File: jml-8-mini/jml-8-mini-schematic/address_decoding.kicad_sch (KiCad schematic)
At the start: 9 parts, among them J5 Address Decoding, U6 74LS04, U7 CD74HCT4514E, U8 74LS139, U9 74LS32

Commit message: change some footprints
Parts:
- U6, U9: footprint Package_DIP:DIP-14_W7.62mm_LongPads -> Package_DIP:DIP-14_W7.62mm_Socket_LongPads
- U7: footprint Package_DIP:DIP-24_W15.24mm_LongPads -> Package_DIP:DIP-24_W15.24mm_Socket_LongPads
- U8: footprint Package_DIP:DIP-16_W7.62mm_LongPads -> Package_DIP:DIP-16_W7.62mm_Socket_LongPads
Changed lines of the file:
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@@
       (effects (font (size 1.27 1.27)))
     )
-    (property "Footprint" "Package_DIP:DIP-14_W7.62mm_LongPads" (at 78.74 46.99 0)
+    (property "Footprint" "Package_DIP:DIP-14_W7.62mm_Socket_LongPads" (at 78.74 46.99 0)
       (effects (font (size 1.27 1.27)) hide)
     )
@@
       (effects (font (size 1.27 1.27)))
     )
-    (property "Footprint" "Package_DIP:DIP-14_W7.62mm_LongPads" (at 116.84 73.66 0)
+    (property "Footprint" "Package_DIP:DIP-14_W7.62mm_Socket_LongPads" (at 116.84 73.66 0)
       (effects (font (size 1.27 1.27)) hide)
     )
@@
       (effects (font (size 1.27 1.27)))
     )
-    (property "Footprint" "Package_DIP:DIP-14_W7.62mm_LongPads" (at 127 104.14 0)
+    (property "Footprint" "Package_DIP:DIP-14_W7.62mm_Socket_LongPads" (at 127 104.14 0)
       (effects (font (size 1.27 1.27)) hide)
     )
@@
       (effects (font (size 1.27 1.27)) (justify left))
     )
-    (property "Footprint" "Package_DIP:DIP-16_W7.62mm_LongPads" (at 256.54 129.54 0)
+    (property "Footprint" "Package_DIP:DIP-16_W7.62mm_Socket_LongPads" (at 256.54 129.54 0)
       (effects (font (size 1.27 1.27)) hide)
     )
@@
       (effects (font (size 1.27 1.27)) (justify left))
     )
-    (property "Footprint" "Package_DIP:DIP-24_W15.24mm_LongPads" (at 21.59 85.09 0)
+    (property "Footprint" "Package_DIP:DIP-24_W15.24mm_Socket_LongPads" (at 21.59 85.09 0)
       (effects (font (size 1.27 1.27)) hide)
     )
@@
       (effects (font (size 1.27 1.27)))
     )
-    (property "Footprint" "Package_DIP:DIP-14_W7.62mm_LongPads" (at 251.46 83.185 0)
+    (property "Footprint" "Package_DIP:DIP-14_W7.62mm_Socket_LongPads" (at 251.46 83.185 0)
       (effects (font (size 1.27 1.27)) hide)
     )
@@
       (effects (font (size 1.27 1.27)))
     )
-    (property "Footprint" "Package_DIP:DIP-14_W7.62mm_LongPads" (at 271.78 83.185 0)
+    (property "Footprint" "Package_DIP:DIP-14_W7.62mm_Socket_LongPads" (at 271.78 83.185 0)
       (effects (font (size 1.27 1.27)) hide)
     )
@@
       (effects (font (size 1.27 1.27)))
     )
-    (property "Footprint" "Package_DIP:DIP-14_W7.62mm_LongPads" (at 143.51 29.21 0)
+    (property "Footprint" "Package_DIP:DIP-14_W7.62mm_Socket_LongPads" (at 143.51 29.21 0)
       (effects (font (size 1.27 1.27)) hide)
     )
@@
       (effects (font (size 1.27 1.27)))
     )
-    (property "Footprint" "Package_DIP:DIP-14_W7.62mm_LongPads" (at 261.62 83.185 0)
+    (property "Footprint" "Package_DIP:DIP-14_W7.62mm_Socket_LongPads" (at 261.62 83.185 0)
       (effects (font (size 1.27 1.27)) hide)
     )
@@
       (effects (font (size 1.27 1.27)) (justify left))
     )
-    (property "Footprint" "Package_DIP:DIP-16_W7.62mm_LongPads" (at 83.82 160.02 0)
+    (property "Footprint" "Package_DIP:DIP-16_W7.62mm_Socket_LongPads" (at 83.82 160.02 0)
       (effects (font (size 1.27 1.27)) hide)
     )
@@
       (effects (font (size 1.27 1.27)))
     )
-    (property "Footprint" "Package_DIP:DIP-14_W7.62mm_LongPads" (at 143.51 44.45 0)
+    (property "Footprint" "Package_DIP:DIP-14_W7.62mm_Socket_LongPads" (at 143.51 44.45 0)
       (effects (font (size 1.27 1.27)) hide)
     )
@@
       (effects (font (size 1.27 1.27)))
     )
-    (property "Footprint" "Package_DIP:DIP-14_W7.62mm_LongPads" (at 241.3 83.185 0)
+    (property "Footprint" "Package_DIP:DIP-14_W7.62mm_Socket_LongPads" (at 241.3 83.185 0)
       (effects (font (size 1.27 1.27)) hide)
     )
@@
       (effects (font (size 1.27 1.27)) (justify left))
     )
-    (property "Footprint" "Package_DIP:DIP-14_W7.62mm_LongPads" (at 262.89 44.45 0)
+    (property "Footprint" "Package_DIP:DIP-14_W7.62mm_Socket_LongPads" (at 262.89 44.45 0)
       (effects (font (size 1.27 1.27)) hide)
     )
@@
       (effects (font (size 1.27 1.27)) (justify left))
     )
-    (property "Footprint" "Package_DIP:DIP-14_W7.62mm_LongPads" (at 237.49 44.45 0)
-      (effects (font (size 1.27 1.27)) hide)
-    )
+    (property "Footprint" "Package_DIP:DIP-14_W7.62mm_Socket_LongPads" (at 237.49 44.45 0)
+      (effects (font (size 1.27 1.27)) hide)
+    )

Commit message: lots of updates to schematic to make pcb routing easier, start on pcb design
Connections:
- net A15: now also U9.1; no longer U9.9
- net A5: now also U7.3 (A1); no longer U7.2 (A0)
- net A6: no longer U7.3 (A1)
- net Q0: now also J5.20 (Pin_20); no longer J5.17 (Pin_17)
- net Q1: now also J5.19 (Pin_19), U9.10; no longer J5.18 (Pin_18), U9.5
- net Q2: now also J5.18 (Pin_18), U9.13; no longer J5.19 (Pin_19), U9.2
- net Q3: now also J5.17 (Pin_17); no longer J5.20 (Pin_20)
- net Y0: now also J5.2 (Pin_2), U9.12, U9.9; no longer J5.1 (Pin_1), U9.1, U9.4
- net Y1: now also J5.4 (Pin_4); no longer J5.2 (Pin_2)
- net Y10: now also J5.10 (Pin_10); no longer J5.11 (Pin_11)
- net Y11: now also J5.9 (Pin_9); no longer J5.12 (Pin_12)
- net Y12: now also J5.3 (Pin_3); no longer J5.13 (Pin_13)
- net Y13: now also J5.1 (Pin_1); no longer J5.14 (Pin_14)
- net Y14: now also J5.6 (Pin_6); no longer J5.15 (Pin_15)
- net Y15: now also J5.5 (Pin_5); no longer J5.16 (Pin_16)
- net Y2: now also J5.11 (Pin_11); no longer J5.3 (Pin_3)
- net Y3: now also J5.12 (Pin_12); no longer J5.4 (Pin_4)
- net Y4: now also J5.13 (Pin_13); no longer J5.5 (Pin_5)
- net Y5: now also J5.14 (Pin_14); no longer J5.6 (Pin_6)
- net Y6: now also J5.15 (Pin_15); no longer J5.7 (Pin_7)
- net Y7: now also J5.16 (Pin_16); no longer J5.8 (Pin_8)
- net Y8: now also J5.8 (Pin_8); no longer J5.9 (Pin_9)
- net Y9: now also J5.7 (Pin_7); no longer J5.10 (Pin_10)
- net ~{CTC}: now also U9.11; no longer U9.3
- net ~{MREQ}: now also U9.2, U9.4; no longer U9.10, U9.12
- net ~{RAM}: now also U9.6; no longer U9.11
- net ~{ROM}: now also U9.3; no longer U9.8
- net ~{SIO}: now also U9.8; no longer U9.6
- net ~{A15}: now reaches U6.2
- net ~{A15}: now also U9.5; no longer U9.13
- new net A4: U7.2 (A0)
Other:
- note added: "Address Decoding Breakout"
- note added: "Power"
- moved on the sheet: U6G, U9E

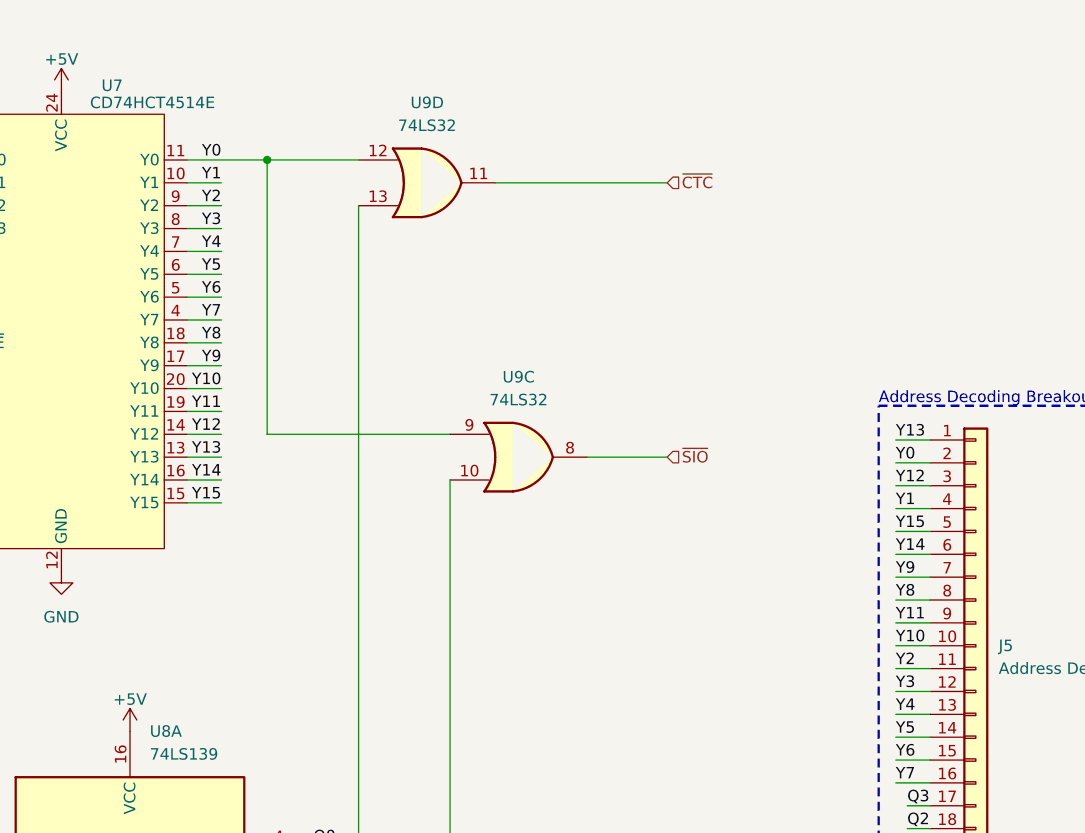
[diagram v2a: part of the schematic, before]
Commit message: fix some errors in schematic/pcb
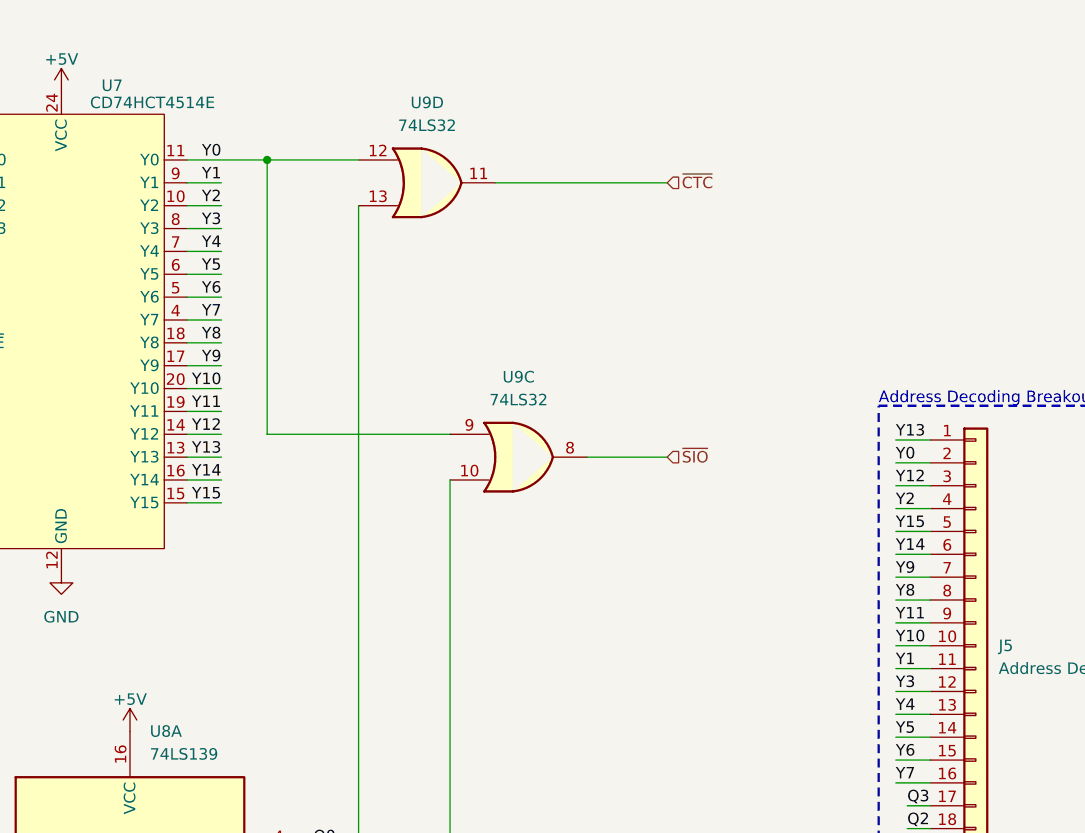
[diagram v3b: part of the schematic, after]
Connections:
- net Y1: now also J5.11 (Pin_11), U7.9 (Y1); no longer J5.4 (Pin_4), U7.10 (Y1)
- net Y2: now also J5.4 (Pin_4), U7.10 (Y2); no longer J5.11 (Pin_11), U7.9 (Y2)
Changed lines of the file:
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@@
     (effects (font (size 1.27 1.27)) (justify right bottom))
   )
-  (label "Y1" (at 168.91 109.855 0) (fields_autoplaced)
+  (label "Y1" (at 168.91 127.635 0) (fields_autoplaced)
     (effects (font (size 1.27 1.27)) (justify left bottom))
   )
@@
     (effects (font (size 1.27 1.27)) (justify left bottom))
   )
-  (label "Y2" (at 168.91 127.635 0) (fields_autoplaced)
+  (label "Y2" (at 168.91 109.855 0) (fields_autoplaced)
     (effects (font (size 1.27 1.27)) (justify left bottom))
   )
@@
     )
     (pin "1")
-    (pin "10")
     (pin "11")
     (pin "12")
@@
     (pin "7")
     (pin "8")
+    (pin "10")
     (pin "9")
     (instances
